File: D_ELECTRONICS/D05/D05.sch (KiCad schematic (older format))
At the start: 34 parts, among them J0 Conn_01x01_Male, J1 Conn_01x01_Male, J2 Conn_01x01_Male, J3 Conn_01x01_Male, J4 Conn_01x10_Female, J6 Conn_01x10_Female

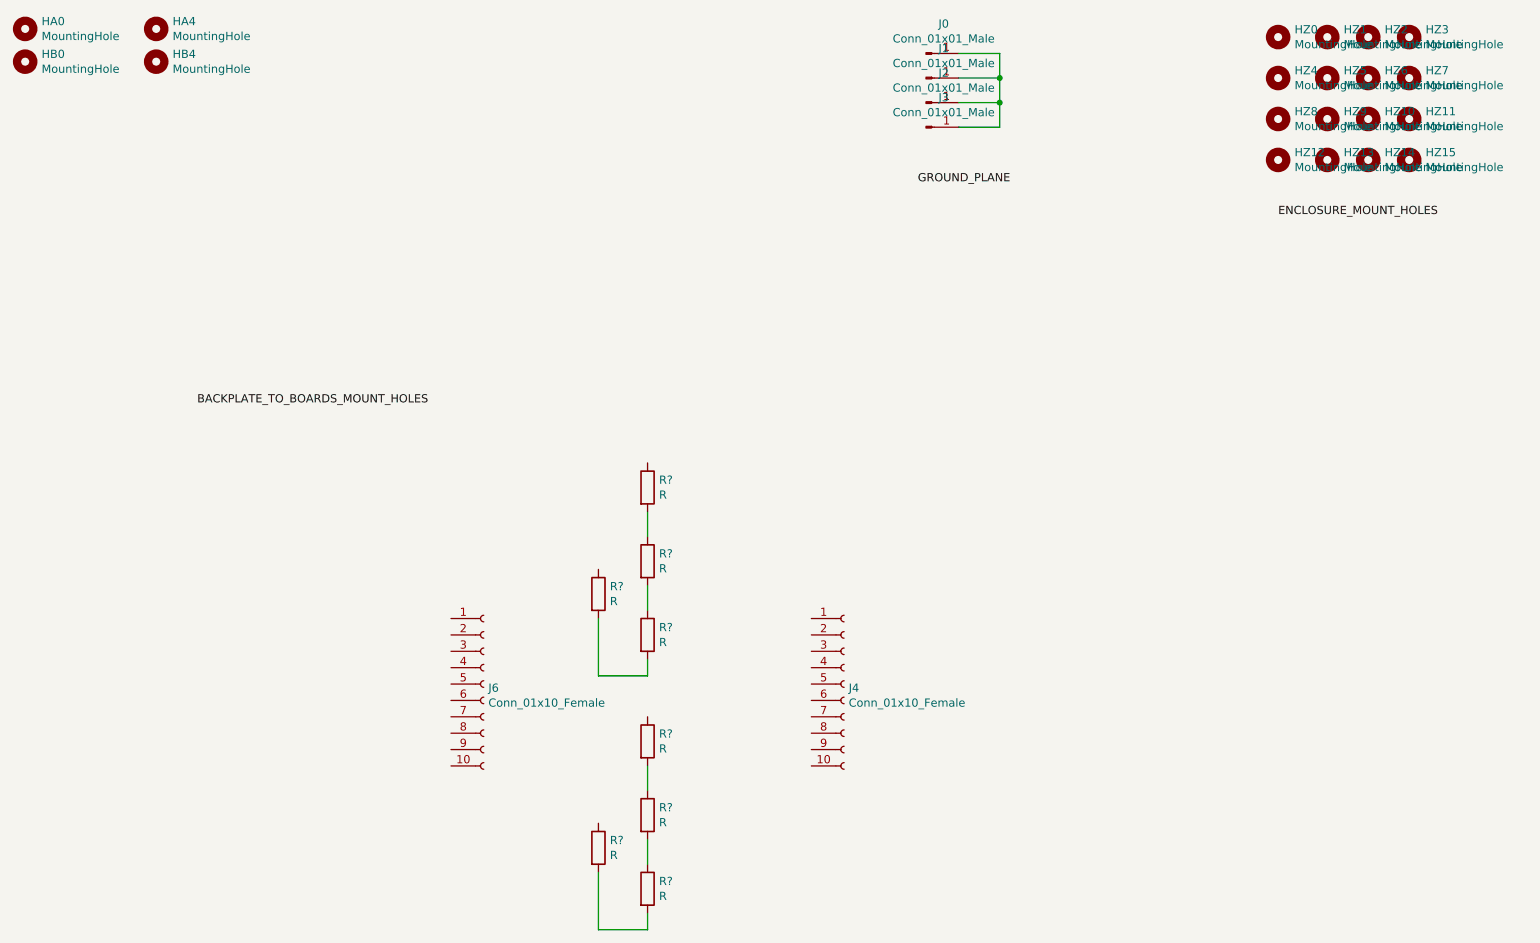
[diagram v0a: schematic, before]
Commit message: all traces routed
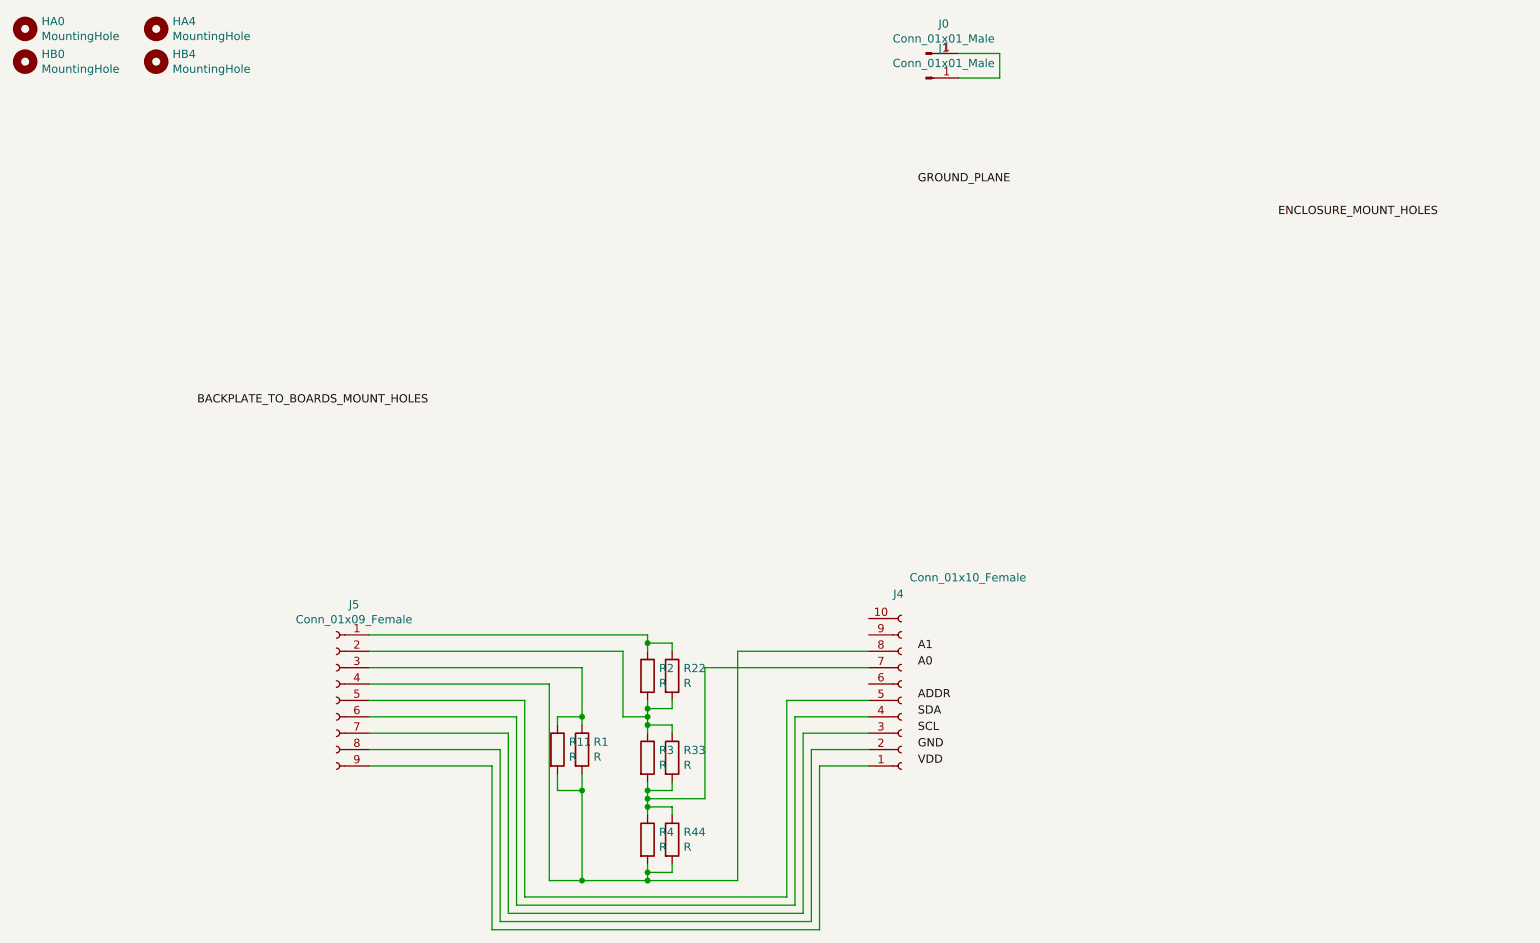
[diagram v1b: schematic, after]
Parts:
- removed HZ0, HZ1, HZ10, HZ11, HZ12, HZ13, HZ14, HZ15, HZ2, HZ3, HZ4, HZ5, HZ6, HZ7, HZ8, HZ9: MountingHole, MountingHole:MountingHole_3mm, symbol Mechanical:MountingHole
- removed J2, J3: Conn_01x01_Male, Connector_Wire:SolderWirePad_1x01_Drill1mm, symbol Connector:Conn_01x01_Male
- removed J6: Conn_01x10_Female, TerminalBlock_4Ucon:TerminalBlock_4Ucon_1x10_P3.50mm_Horizontal, symbol Connector:Conn_01x10_Female
- removed R? (x4): R, symbol Device:R
- added J5: Conn_01x09_Female, TerminalBlock_4Ucon:TerminalBlock_4Ucon_1x09_P3.50mm_Horizontal, symbol Connector:Conn_01x09_Female
- added R11, R22, R33, R44: R, Resistor_SMD:R_0805_2012Metric_Pad1.15x1.40mm_HandSolder, symbol Device:R
- R1, R2, R3, R4: renamed from R?; footprint (none) -> Resistor_THT:R_Axial_DIN0204_L3.6mm_D1.6mm_P2.54mm_Vertical
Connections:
- net at J4.1 (Pin_1): now also J5.9 (Pin_9)
- net at J4.2 (Pin_2): now also J5.8 (Pin_8)
- net at J4.3 (Pin_3): now also J5.7 (Pin_7)
- net at J4.4 (Pin_4): now also J5.6 (Pin_6)
- net at J4.5 (Pin_5): now also J5.5 (Pin_5)
- net at J4.7 (Pin_7): now also R3.2, R4.1, R33.2, R44.1
- net at J4.8 (Pin_8): now also R1.2, R4.2, J5.4 (Pin_4), R11.2, R44.2
- net at R2.2, R3.1: now also J5.2 (Pin_2), R22.2, R33.1
- net at R1.1: now also J5.3 (Pin_3), R11.1
- net at R2.1: now also J5.1 (Pin_1), R22.1
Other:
- moved on the sheet: J4, R1, R2, R3, R4
